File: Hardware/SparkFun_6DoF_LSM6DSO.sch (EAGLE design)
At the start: 31 parts, among them J1 QWIIC_RIGHT_ANGLE, J2 QWIIC_RIGHT_ANGLE, U1 LSM6DS0

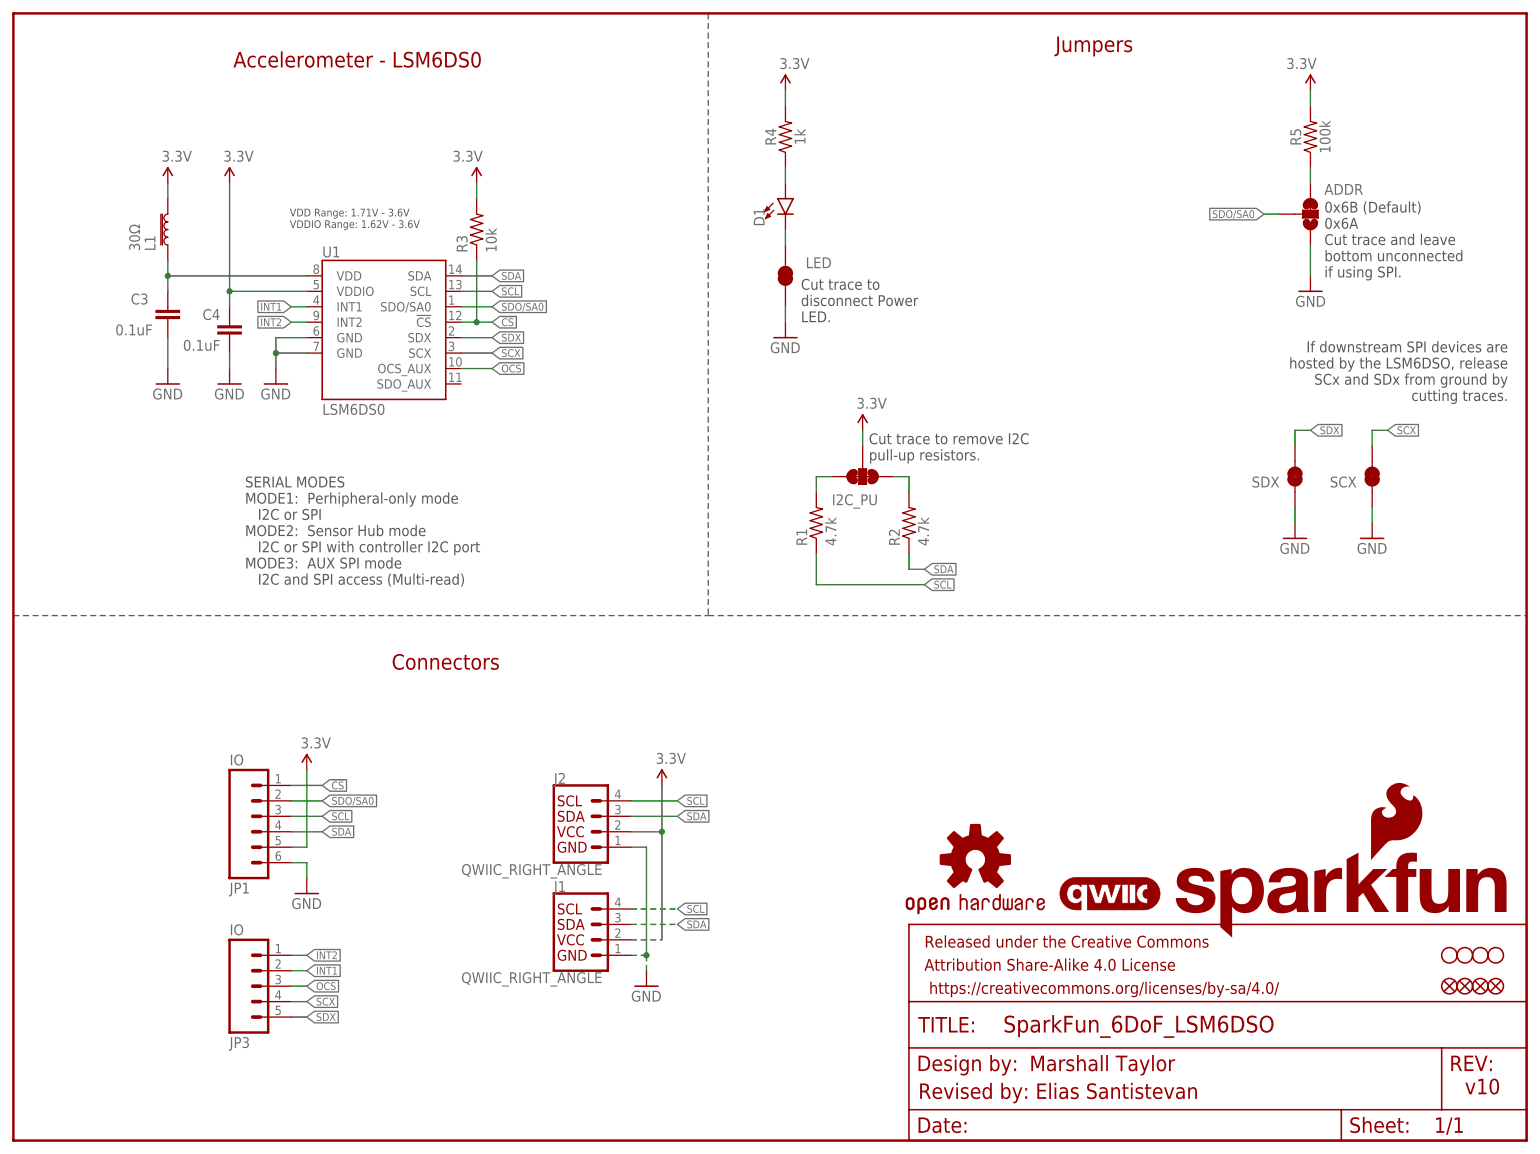
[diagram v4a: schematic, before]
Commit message: Adds SDO_AUX to header, updates symbol to have more consistent labeling
* Approves some minor DRC errors
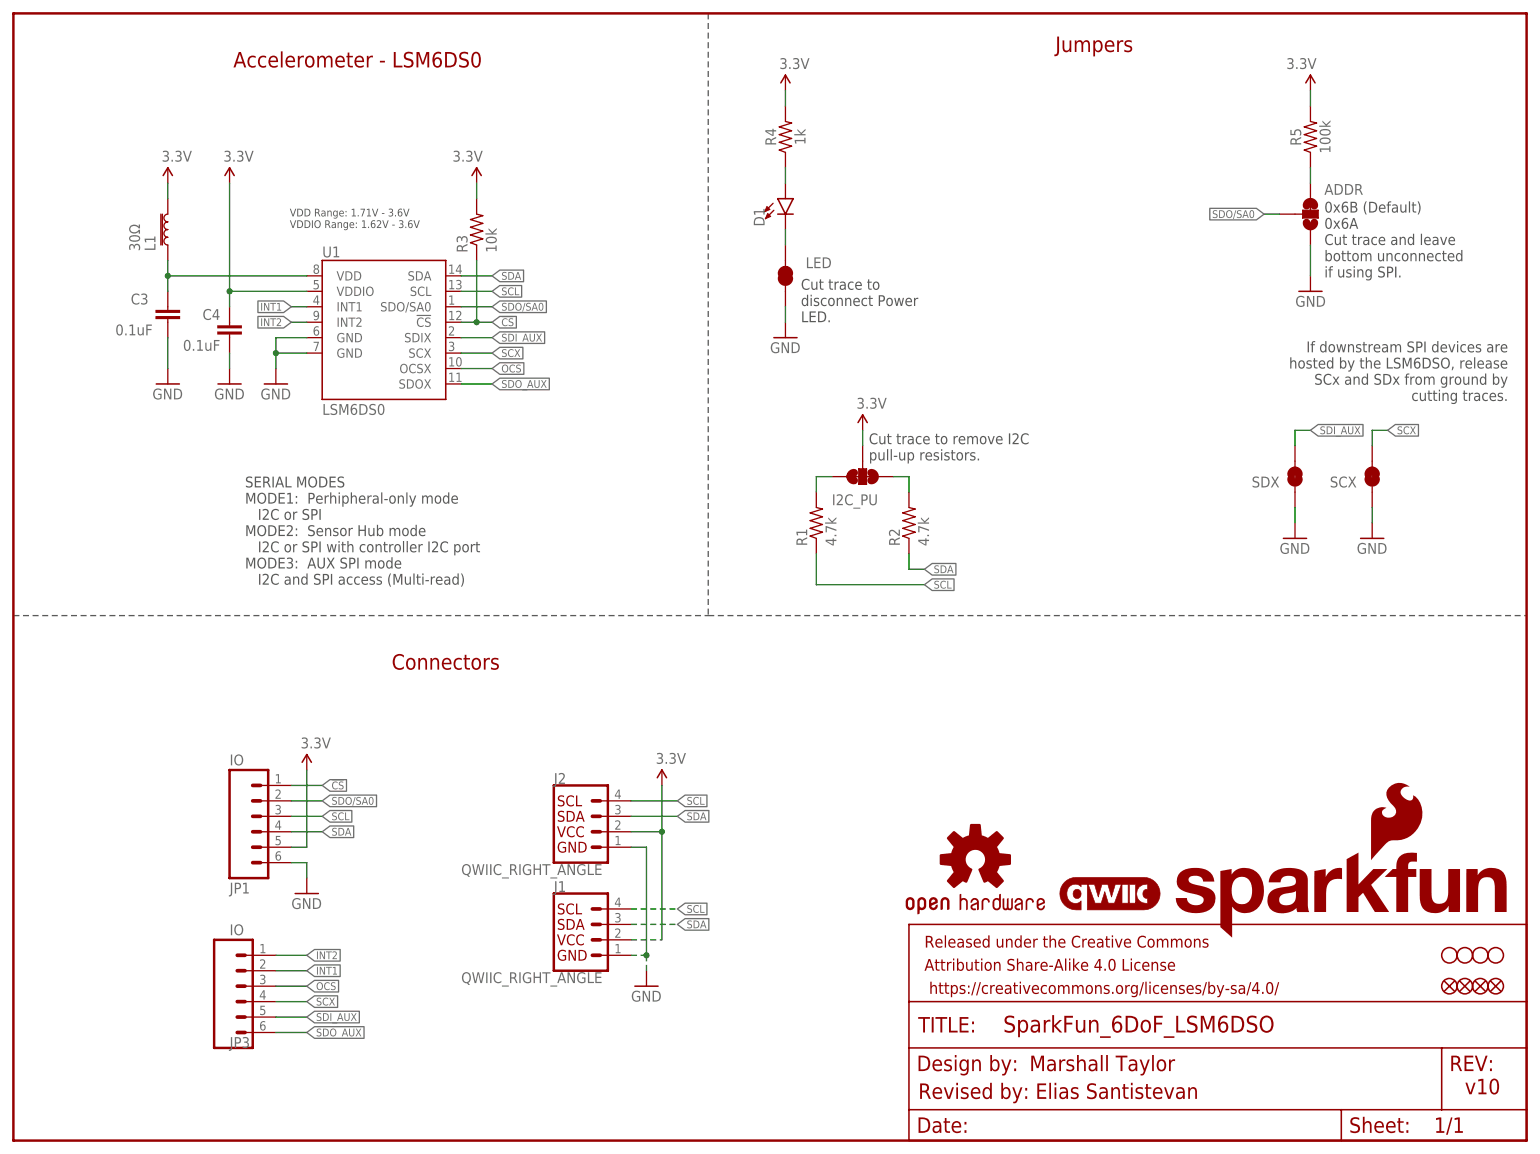
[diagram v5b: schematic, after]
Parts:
- JP3: device SparkFun-Connectors:CONN_05NO_SILK -> SparkFun-Connectors:CONN_06NO_SILK_NO_POP
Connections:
- removed net SDX: JP3.5, SDX.2, U1.SDX
- new net SDI_AUX: JP3.5, SDX.2, U1.SDIX
- new net SDO_AUX: JP3.6, U1.SDOX
- net OCS: now also U1.OCSX; no longer U1.OCS_AUX
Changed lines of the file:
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@@
 <part name="SCX" library="SparkFun-Jumpers" deviceset="JUMPER-SMT_2_NC_TRACE" device="_SILK" package3d_urn="urn:adsk.eagle:package:39281/1"/>
 <part name="LOGO3" library="SparkFun-Aesthetics" deviceset="SFE_LOGO_NAME_FLAME" device=".1_INCH" value="SFE_LOGO_NAME_FLAME.1_INCH"/>
-<part name="JP3" library="SparkFun-Connectors" deviceset="CONN_05" device="NO_SILK" value="IO"/>
+<part name="JP3" library="SparkFun-Connectors" deviceset="CONN_06" device="NO_SILK_NO_POP" value="IO"/>
 <part name="J1" library="SparkFun-Connectors" deviceset="QWIIC_CONNECTOR" device="JS-1MM" value="QWIIC_RIGHT_ANGLE"/>
 <part name="FD1" library="SparkFun-Aesthetics" deviceset="FIDUCIAL" device="UFIDUCIAL"/>
@@
 </segment>
 </net>
-<net name="SDX" class="0">
+<net name="SDI_AUX" class="0">
 <segment>
 <pinref part="JP3" gate="G$1" pin="5"/>
-<wire x1="45.72" y1="20.32" x2="48.26" y2="20.32" width="0.1524" layer="91"/>
+<wire x1="43.18" y1="20.32" x2="48.26" y2="20.32" width="0.1524" layer="91"/>
 <label x="48.26" y="20.32" size="1.27" layer="95" font="vector" xref="yes"/>
 </segment>
@@
 <wire x1="73.66" y1="132.08" x2="78.74" y2="132.08" width="0.1524" layer="91"/>
 <label x="78.74" y="132.08" size="1.27" layer="95" font="vector" xref="yes"/>
-<pinref part="U1" gate="G$1" pin="SDX"/>
+<pinref part="U1" gate="G$1" pin="SDIX"/>
 </segment>
 <segment>
@@
 <segment>
 <pinref part="JP3" gate="G$1" pin="4"/>
-<wire x1="45.72" y1="22.86" x2="48.26" y2="22.86" width="0.1524" layer="91"/>
+<wire x1="43.18" y1="22.86" x2="48.26" y2="22.86" width="0.1524" layer="91"/>
 <label x="48.26" y="22.86" size="1.27" layer="95" font="vector" xref="yes"/>
 </segment>
@@
 <segment>
 <pinref part="JP3" gate="G$1" pin="2"/>
-<wire x1="45.72" y1="27.94" x2="48.26" y2="27.94" width="0.1524" layer="91"/>
+<wire x1="43.18" y1="27.94" x2="48.26" y2="27.94" width="0.1524" layer="91"/>
 <label x="48.26" y="27.94" size="1.27" layer="95" font="vector" xref="yes"/>
 </segment>
@@
 <segment>
 <pinref part="JP3" gate="G$1" pin="1"/>
-<wire x1="45.72" y1="30.48" x2="48.26" y2="30.48" width="0.1524" layer="91"/>
+<wire x1="43.18" y1="30.48" x2="48.26" y2="30.48" width="0.1524" layer="91"/>
 <label x="48.26" y="30.48" size="1.27" layer="95" font="vector" xref="yes"/>
 </segment>
@@
 <wire x1="73.66" y1="127" x2="78.74" y2="127" width="0.1524" layer="91"/>
 <label x="78.74" y="127" size="1.27" layer="95" font="vector" xref="yes"/>
-<pinref part="U1" gate="G$1" pin="OCS_AUX"/>
+<pinref part="U1" gate="G$1" pin="OCSX"/>
 </segment>
 <segment>
 <pinref part="JP3" gate="G$1" pin="3"/>
-<wire x1="45.72" y1="25.4" x2="48.26" y2="25.4" width="0.1524" layer="91"/>
+<wire x1="43.18" y1="25.4" x2="48.26" y2="25.4" width="0.1524" layer="91"/>
 <label x="48.26" y="25.4" size="1.27" layer="95" font="vector" xref="yes"/>
 </segment>
@@
 </segment>
 </net>
+<net name="SDO_AUX" class="0">
+<segment>
+<pinref part="U1" gate="G$1" pin="SDOX"/>
+<wire x1="73.66" y1="124.46" x2="78.74" y2="124.46" width="0.1524" layer="91"/>
+<label x="78.74" y="124.46" size="1.27" layer="95" xref="yes"/>
+</segment>
+<segment>
+<pinref part="JP3" gate="G$1" pin="6"/>
+<wire x1="43.18" y1="17.78" x2="48.26" y2="17.78" width="0.1524" layer="91"/>
+<label x="48.26" y="17.78" size="1.27" layer="95" xref="yes"/>
+</segment>
+</net>

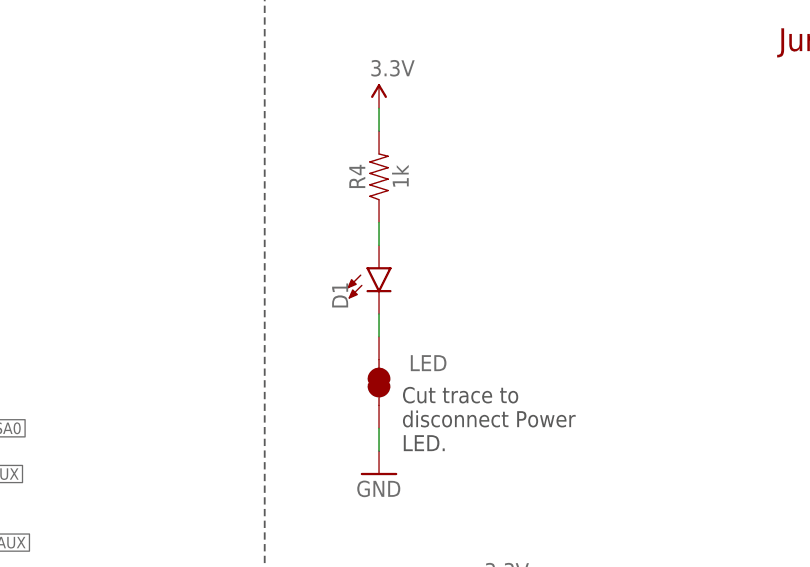
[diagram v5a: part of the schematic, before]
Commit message: Adds red LED with PROD_ID to schematic
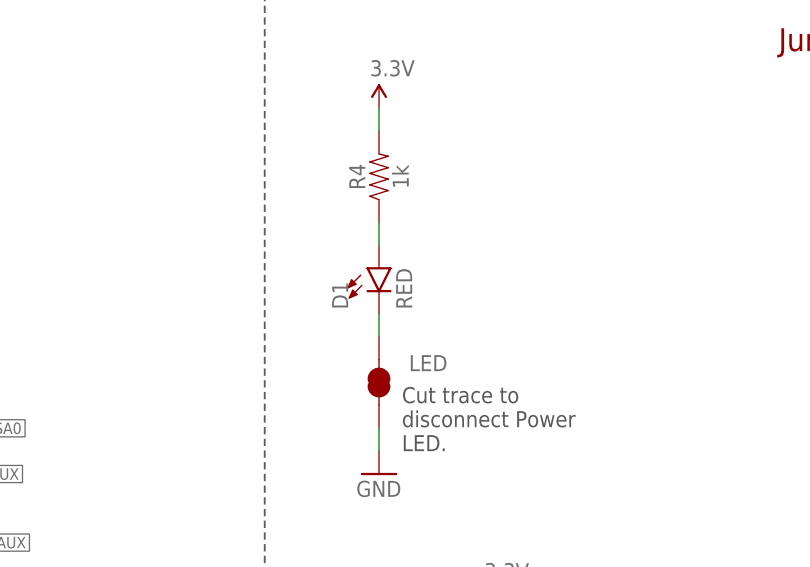
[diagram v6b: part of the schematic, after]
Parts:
- D1: value (none) -> RED; device SparkFun-LED:LED0603 -> SparkFun-LED:LED-RED0603
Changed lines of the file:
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@@
 <part name="GND3" library="SparkFun-PowerSymbols" deviceset="GND" device=""/>
 <part name="J2" library="SparkFun-Connectors" deviceset="QWIIC_CONNECTOR" device="JS-1MM" value="QWIIC_RIGHT_ANGLE"/>
-<part name="D1" library="SparkFun-LED" deviceset="LED" device="0603"/>
+<part name="D1" library="SparkFun-LED" deviceset="LED-RED" device="0603" value="RED"/>
 <part name="R4" library="SparkFun-Resistors" deviceset="1KOHM" device="-0603-1/10W-1%" value="1k"/>
 <part name="LED" library="SparkFun-Jumpers" deviceset="JUMPER-SMT_2_NC_TRACE" device="_SILK" package3d_urn="urn:adsk.eagle:package:39281/1"/>
@@
 <attribute name="NAME" x="88.9" y="58.674" size="1.778" layer="95" font="vector"/>
 </instance>
-<instance part="D1" gate="D1" x="127" y="154.94" smashed="yes">
+<instance part="D1" gate="G$1" x="127" y="154.94" smashed="yes">
 <attribute name="NAME" x="123.571" y="150.368" size="1.778" layer="95" font="vector" rot="R90"/>
 <attribute name="VALUE" x="128.905" y="150.368" size="1.778" layer="96" font="vector" rot="R90" align="top-left"/>
@@
 <segment>
 <pinref part="R4" gate="G$1" pin="1"/>
-<pinref part="D1" gate="D1" pin="A"/>
+<pinref part="D1" gate="G$1" pin="A"/>
 <wire x1="127" y1="160.02" x2="127" y2="157.48" width="0.1524" layer="91"/>
 </segment>
@@
 <net name="N$3" class="0">
 <segment>
-<pinref part="D1" gate="D1" pin="C"/>
+<pinref part="D1" gate="G$1" pin="C"/>
 <pinref part="LED" gate="G$1" pin="2"/>
 <wire x1="127" y1="149.86" x2="127" y2="147.32" width="0.1524" layer="91"/>

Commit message: Removes temp library and uses LSM6DSO IC from SparkFun Eagle Libraries.
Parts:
- U1: device temp:LSM6DS0 -> SparkFun-Sensors:LSM6DSO
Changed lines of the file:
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@@
 <part name="SUPPLY3" library="SparkFun-PowerSymbols" deviceset="3.3V" device=""/>
 <part name="GND7" library="SparkFun-PowerSymbols" deviceset="GND" device=""/>
-<part name="U1" library="temp" deviceset="LSM6DS0" device="" value="LSM6DS0"/>
+<part name="U1" library="SparkFun-Sensors" deviceset="LSM6DSO" device="" value="LSM6DS0"/>
 <part name="STANDOFF4" library="SparkFun-Hardware" deviceset="STAND-OFF" device="TIGHT"/>
 <part name="R5" library="SparkFun-Resistors" deviceset="100KOHM" device="-0603-1/10W-1%" value="100k"/>
